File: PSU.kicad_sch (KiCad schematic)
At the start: 24 parts

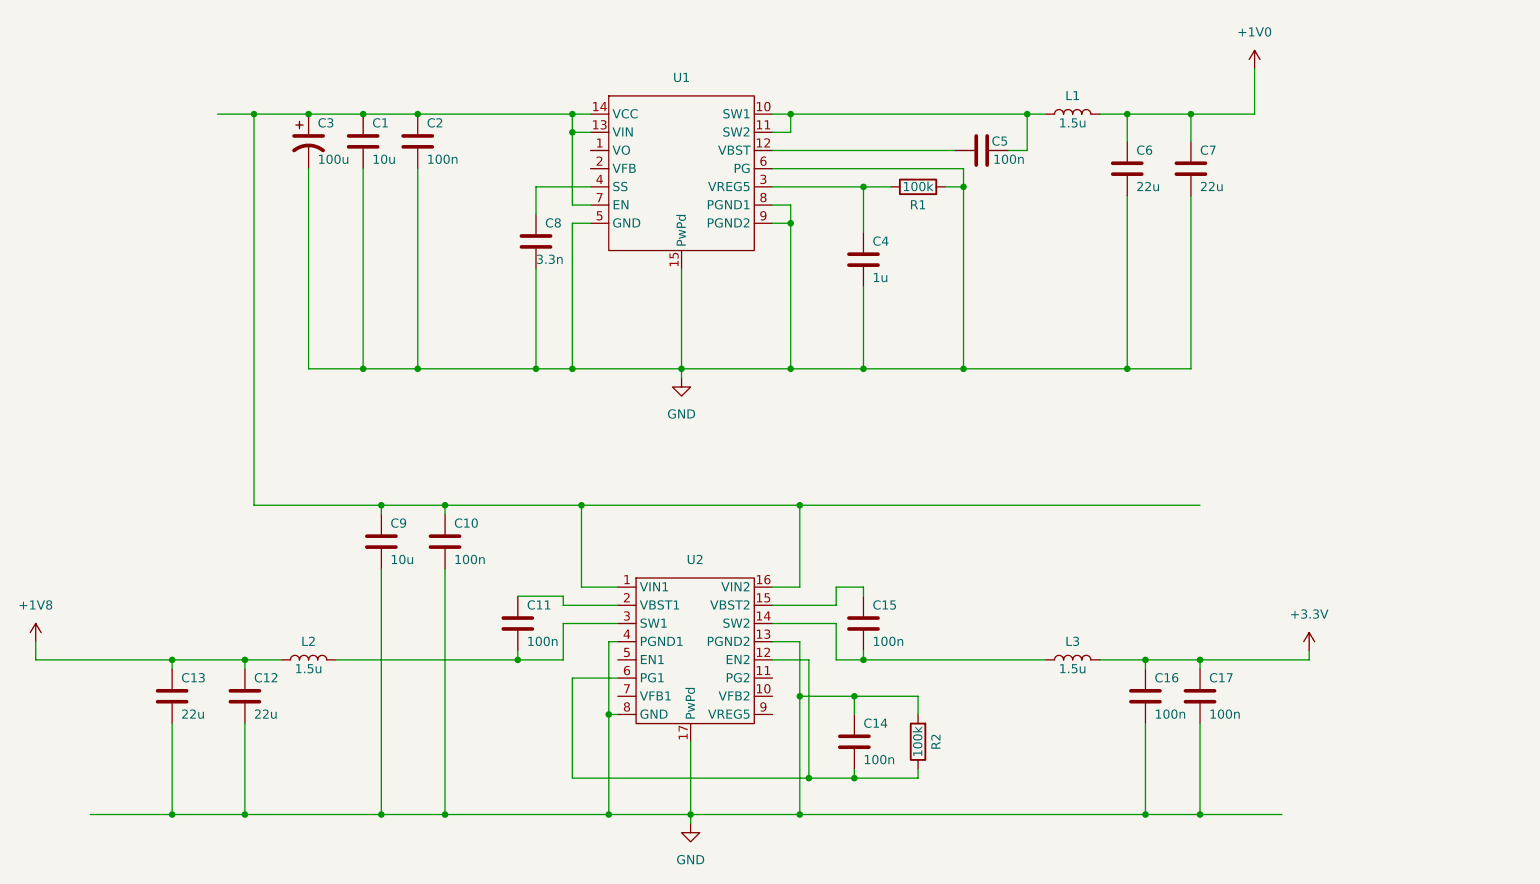
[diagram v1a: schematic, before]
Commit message: Finished PSU schematic
Finish first draft of the PSU schematic. Subject to change
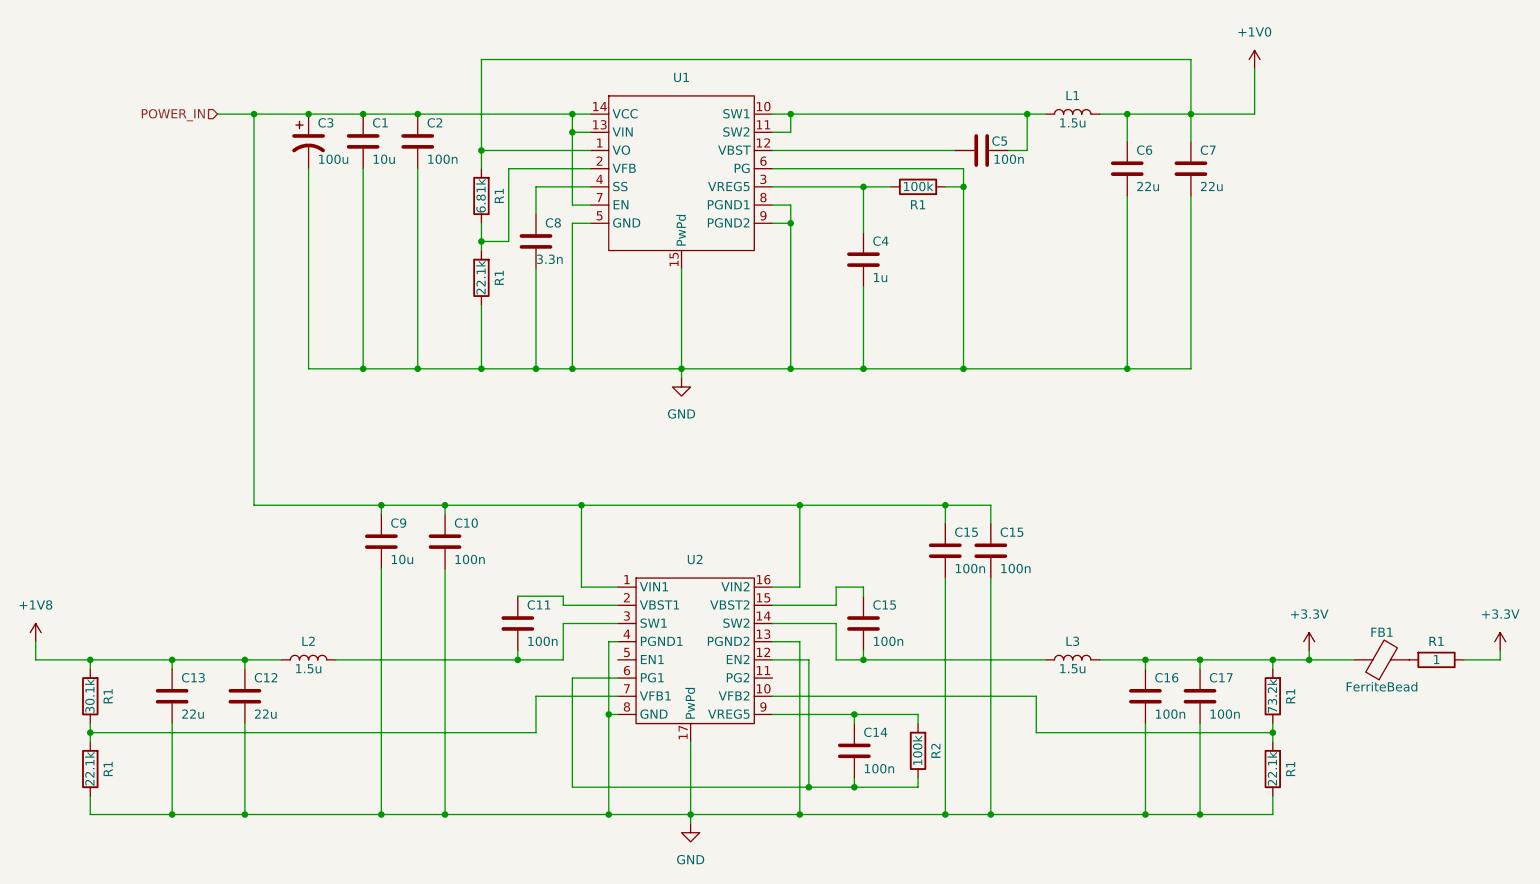
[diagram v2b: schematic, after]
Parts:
- added C15 (x2): 100n, symbol Device:C
- added FB1: FerriteBead, symbol Device:FerriteBead
- added R1 (x3): 22.1k, symbol Device:R
- added R1: 73.2k, symbol Device:R
- added R1: 1, symbol Device:R
- added R1: 30.1k, symbol Device:R
- added R1: 6.81k, symbol Device:R
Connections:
- net +1V0: now also U1.1 (VO), R1.2
- net +1V8: now also R1.2
- net +3.3V: now also FB1.1, R1.1, R1.2
- net GND: now also C15.2, C15.2, R1.1, R1.1, R1.1; no longer C14.1, R2.2
- net POWER_IN: now reaches C1.1, C10.1, C2.1, C3.1, C9.1, U1.13 (VIN), U1.14 (VCC), U1.7 (EN), U2.1 (VIN1), U2.16 (VIN2)
- net POWER_IN: now also C15.1, C15.1
- net at U2.10 (VFB2): now also R1.1, R1.2
- net at U2.7 (VFB1): now also R1.1, R1.2
- net at U2.9 (VREG5): now also C14.1, R2.2
- net at U1.2 (VFB): now also R1.1, R1.2
- new net: FB1.2, R1.2
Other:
- moved on the sheet: C14, R2

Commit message: Fixed wrong capacitor values
Some capacitor values were wrong, they have now been fixed
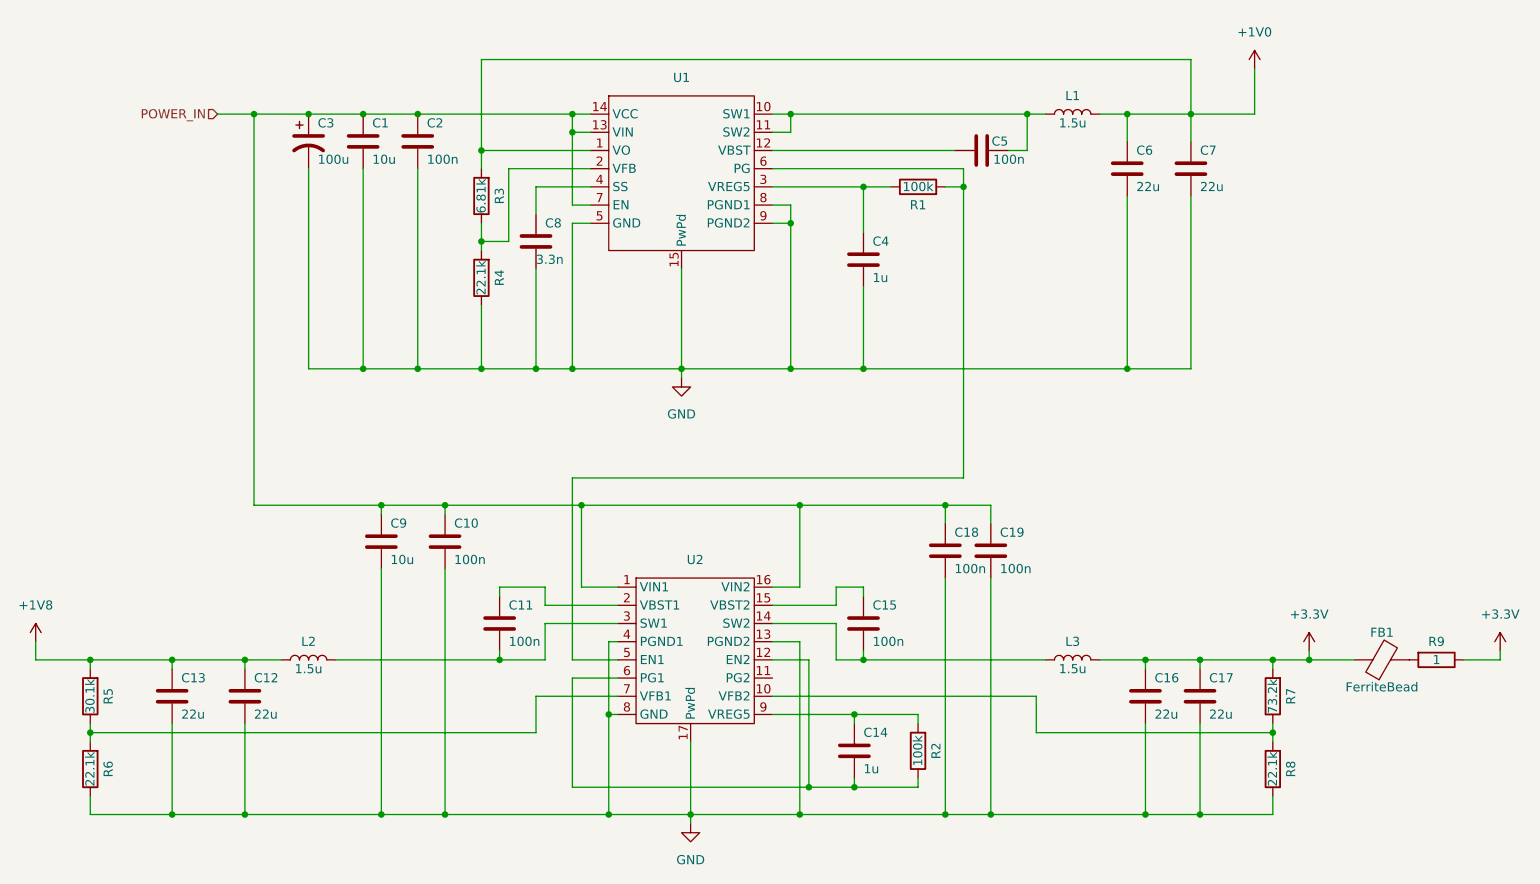
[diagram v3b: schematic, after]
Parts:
- C14: value 100n -> 1u
- C16, C17: value 100n -> 22u
- renumbered C15 to C18, C15 to C19, R1 to R3, R1 to R4, R1 to R5, R1 to R6, R1 to R7, R1 to R8, R1 to R9
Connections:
- net GND: no longer R1.2, U1.6 (PG)
- net at U2.5 (EN1): now also R1.2, U1.6 (PG)
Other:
- moved on the sheet: C11

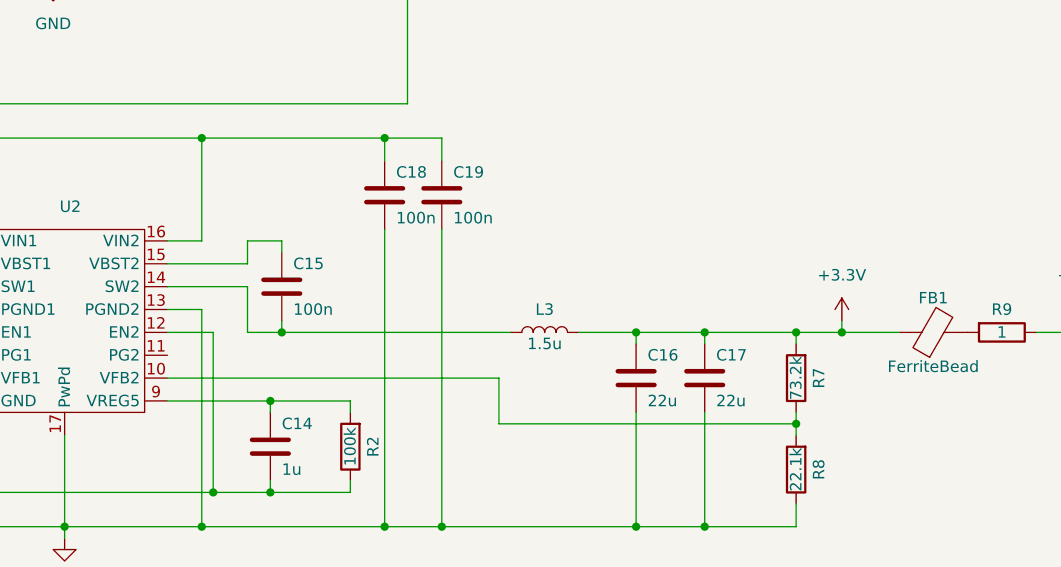
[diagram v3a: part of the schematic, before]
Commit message: Fixed more wrong values in capacitors and resistors
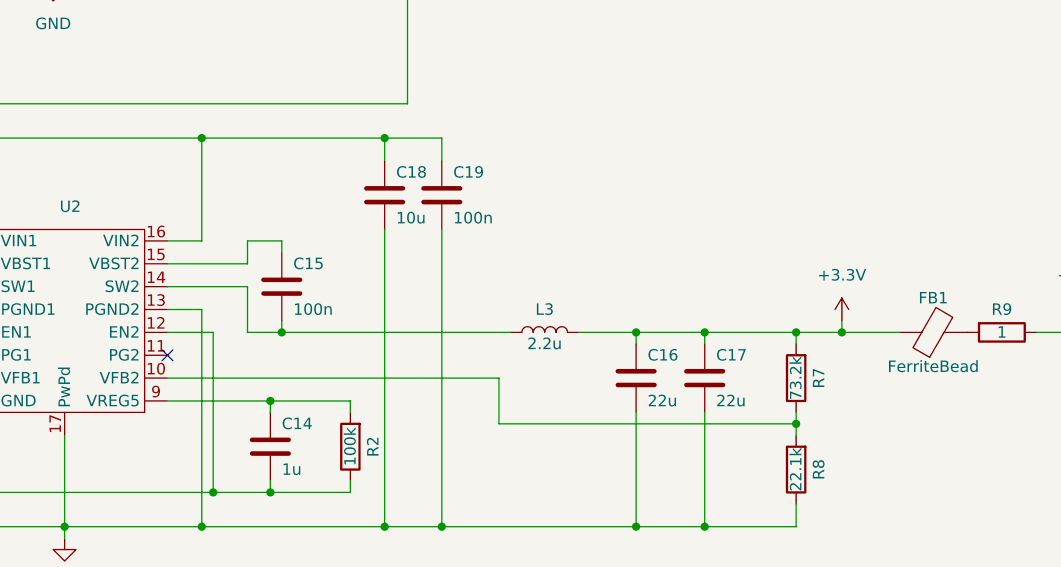
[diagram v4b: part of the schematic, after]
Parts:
- C18: value 100n -> 10u
- L3: value 1.5u -> 2.2u
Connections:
- no-connect marks 0 -> 1

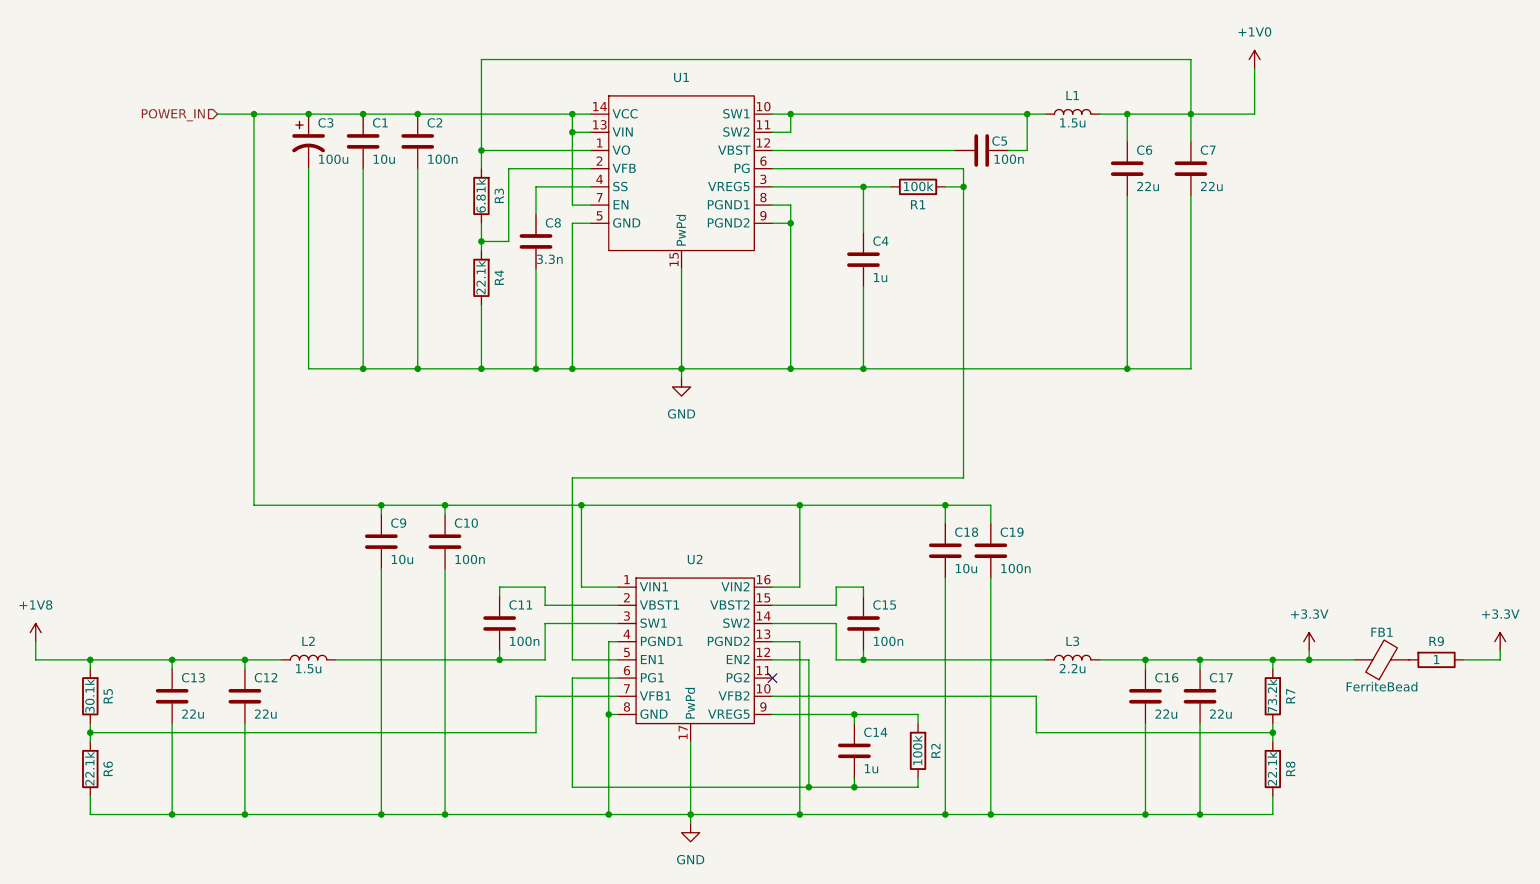
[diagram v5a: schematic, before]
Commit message: Changed PSU power pins to hierachical labels
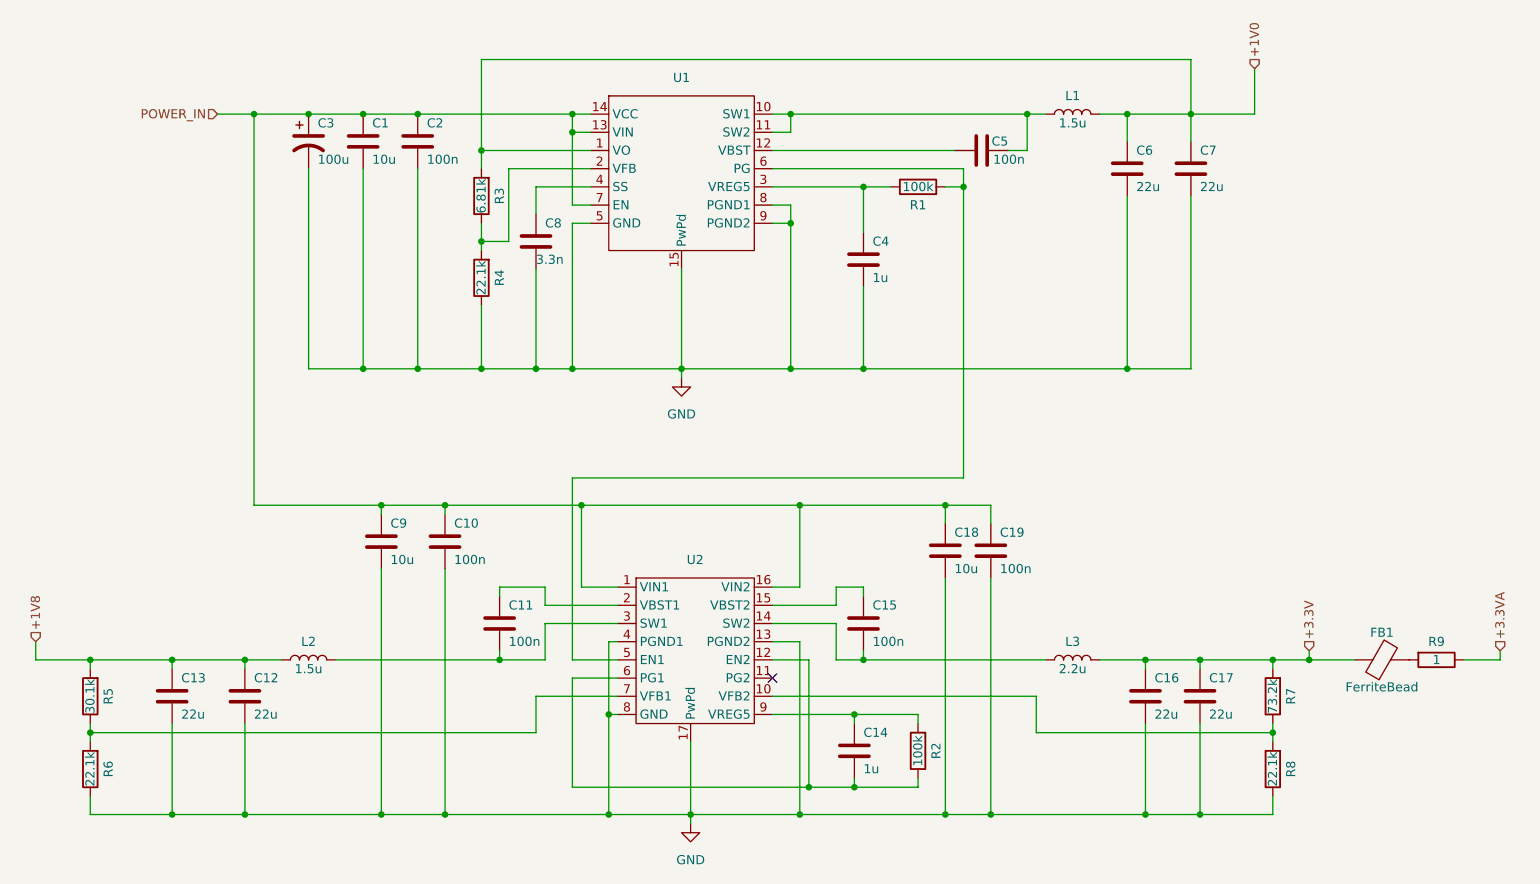
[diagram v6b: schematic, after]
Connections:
- net +3.3V: no longer R9.1
- new net +3.3VA: R9.1
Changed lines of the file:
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@@
     (stroke (width 0) (type default))
+  )
+  (hierarchical_label "+3.3V" (shape input) (at 241.3 129.54 90) (fields_autoplaced)
+    (effects (font (size 1.27 1.27)) (justify left))
+  )
+  (hierarchical_label "+1V8" (shape input) (at 63.5 128.27 90) (fields_autoplaced)
+    (effects (font (size 1.27 1.27)) (justify left))
   )
   (hierarchical_label "POWER_IN" (shape input) (at 88.9 54.61 180)
@@
     )
   )
+  (hierarchical_label "+3.3VA" (shape input) (at 267.97 129.54 90) (fields_autoplaced)
+    (effects (font (size 1.27 1.27)) (justify left))
+  )
+  (hierarchical_label "+1V0" (shape input) (at 233.68 48.26 90) (fields_autoplaced)
+    (effects (font (size 1.27 1.27)) (justify left))
+  )
   (symbol (lib_id "Device:L") (at 101.6 130.81 90) (unit 1)
     (in_bom yes) (on_board yes) (dnp no)
@@
         (path "/fba50eda-8593-4456-af98-ff56fd418a76/2f5e5303-1176-466f-800a-96bac7c62873"
           (reference "#PWR01") (unit 1)
-        )
-      )
-    )
-  )
-  (symbol (lib_id "power:+3.3V") (at 241.3 129.54 0) (unit 1)
-    (in_bom yes) (on_board yes) (dnp no) (fields_autoplaced)
-    (property "Reference" "#PWR04" (at 241.3 133.35 0)
-      (effects (font (size 1.27 1.27)) hide)
-    )
-    (property "Value" "+3.3V" (at 241.3 124.46 0)
-      (effects (font (size 1.27 1.27)))
-    )
-    (property "Footprint" "" (at 241.3 129.54 0)
-      (effects (font (size 1.27 1.27)) hide)
-    )
-    (property "Datasheet" "" (at 241.3 129.54 0)
-      (effects (font (size 1.27 1.27)) hide)
-    )
-    (pin "1")
-    (instances
-      (project "GuitarZero"
-        (path "/fba50eda-8593-4456-af98-ff56fd418a76/2f5e5303-1176-466f-800a-96bac7c62873"
-          (reference "#PWR04") (unit 1)
         )
       )
@@
     )
   )
-  (symbol (lib_id "power:+1V0") (at 233.68 48.26 0) (unit 1)
-    (in_bom yes) (on_board yes) (dnp no) (fields_autoplaced)
-    (property "Reference" "#PWR03" (at 233.68 52.07 0)
-      (effects (font (size 1.27 1.27)) hide)
-    )
-    (property "Value" "+1V0" (at 233.68 43.18 0)
-      (effects (font (size 1.27 1.27)))
-    )
-    (property "Footprint" "" (at 233.68 48.26 0)
-      (effects (font (size 1.27 1.27)) hide)
-    )
-    (property "Datasheet" "" (at 233.68 48.26 0)
-      (effects (font (size 1.27 1.27)) hide)
-    )
-    (pin "1")
-    (instances
-      (project "GuitarZero"
-        (path "/fba50eda-8593-4456-af98-ff56fd418a76/2f5e5303-1176-466f-800a-96bac7c62873"
-          (reference "#PWR03") (unit 1)
-        )
-      )
-    )
-  )
   (symbol (lib_id "Device:C") (at 177.8 143.51 0) (unit 1)
     (in_bom yes) (on_board yes) (dnp no)
@@
     )
   )
-  (symbol (lib_id "power:+3.3V") (at 267.97 129.54 0) (unit 1)
-    (in_bom yes) (on_board yes) (dnp no) (fields_autoplaced)
-    (property "Reference" "#PWR06" (at 267.97 133.35 0)
-      (effects (font (size 1.27 1.27)) hide)
-    )
-    (property "Value" "+3.3V" (at 267.97 124.46 0)
-      (effects (font (size 1.27 1.27)))
-    )
-    (property "Footprint" "" (at 267.97 129.54 0)
-      (effects (font (size 1.27 1.27)) hide)
-    )
-    (property "Datasheet" "" (at 267.97 129.54 0)
-      (effects (font (size 1.27 1.27)) hide)
-    )
-    (pin "1")
-    (instances
-      (project "GuitarZero"
-        (path "/fba50eda-8593-4456-af98-ff56fd418a76/2f5e5303-1176-466f-800a-96bac7c62873"
-          (reference "#PWR06") (unit 1)
-        )
-      )
-    )
-  )
   (symbol (lib_id "Device:C") (at 224.79 62.23 0) (unit 1)
     (in_bom yes) (on_board yes) (dnp no)
@@
         )
       )
-    )
-  )
-  (symbol (lib_id "power:+1V8") (at 63.5 128.27 0) (unit 1)
-    (in_bom yes) (on_board yes) (dnp no) (fields_autoplaced)
-    (property "Reference" "#PWR05" (at 63.5 132.08 0)
-      (effects (font (size 1.27 1.27)) hide)
-    )
-    (property "Value" "+1V8" (at 63.5 123.19 0)
-      (effects (font (size 1.27 1.27)))
-    )
-    (property "Footprint" "" (at 63.5 128.27 0)
-      (effects (font (size 1.27 1.27)) hide)
-    )
-    (property "Datasheet" "" (at 63.5 128.27 0)
-      (effects (font (size 1.27 1.27)) hide)
-    )
-    (pin "1")
-    (instances
-      (project "GuitarZero"
-        (path "/fba50eda-8593-4456-af98-ff56fd418a76/2f5e5303-1176-466f-800a-96bac7c62873"
-          (reference "#PWR05") (unit 1)
-        )
-      )
